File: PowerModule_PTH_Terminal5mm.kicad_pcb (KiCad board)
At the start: 2 copper layers, 26.3 x 20 mm, 5 parts, among them J1 Conn_01x05, J2 Conn_01x05, J3 Screw_Terminal

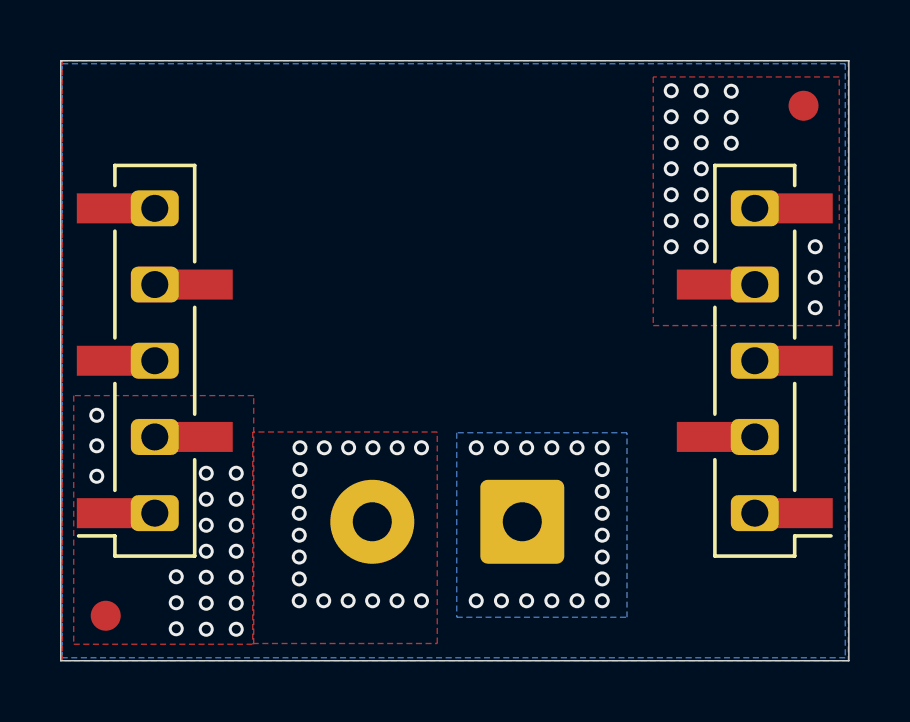
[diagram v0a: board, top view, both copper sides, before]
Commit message: Increase header connectors paste openning by 5%. Decrease screw terminal holes from 2.3mm to 2.2mm.
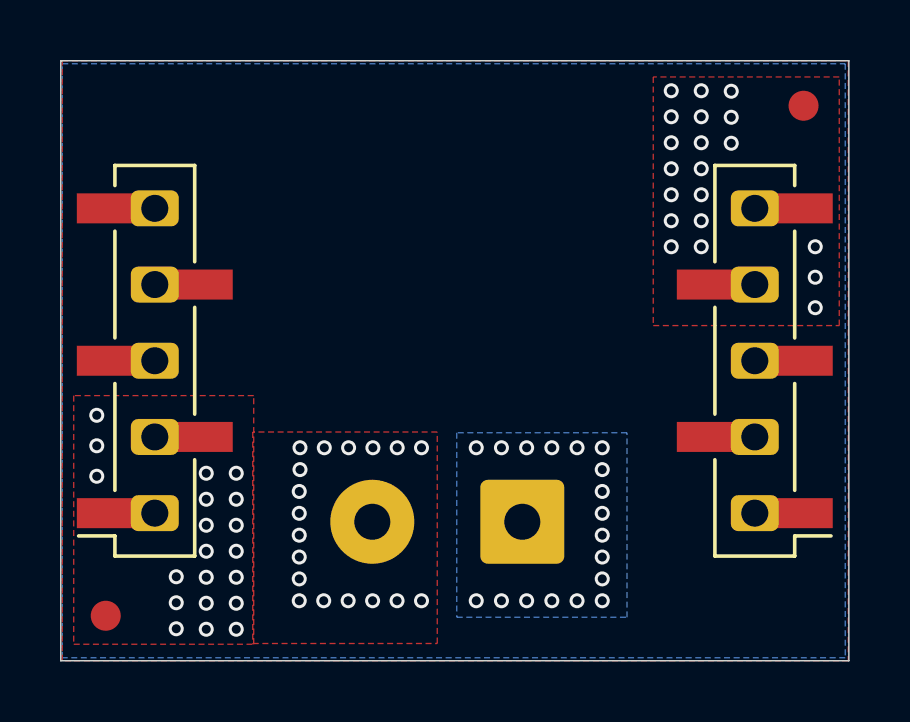
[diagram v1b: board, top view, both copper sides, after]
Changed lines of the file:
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@@
 	(net 3 "unconnected-(J1-Pin_3-Pad3)")
 	(net 4 "unconnected-(J2-Pin_3-Pad3)")
-	(net 5 "unconnected-(J2-Pin_3-Pad3)_1")
-	(net 6 "unconnected-(J1-Pin_3-Pad3)_1")
 	(footprint "Fiducial:Fiducial_1mm_Mask2mm"
 		(locked yes)
@@
 		(sheetname "Root")
 		(sheetfile "PowerModule_PTH_Terminal5mm.kicad_sch")
+		(solder_paste_ratio 0.05)
 		(attr smd)
 		(fp_line
@@
 			(size 1.6 1.2)
 			(drill 0.9)
-			(layers "*.Cu" "*.Mask")
+			(layers "*.Cu" "*.Mask" "In1.Cu" "In2.Cu" "In3.Cu" "In4.Cu" "In5.Cu" "In6.Cu"
+				"In7.Cu" "In8.Cu" "In9.Cu" "In10.Cu" "In11.Cu" "In12.Cu" "In13.Cu" "In14.Cu"
+				"In15.Cu" "In16.Cu" "In17.Cu" "In18.Cu" "In19.Cu" "In20.Cu" "In21.Cu"
+				"In22.Cu" "In23.Cu" "In24.Cu" "In25.Cu" "In26.Cu" "In27.Cu" "In28.Cu"
+				"In29.Cu" "In30.Cu"
+			)
 			(remove_unused_layers no)
 			(roundrect_rratio 0.2083333333)
@@
 			(size 1.6 1.2)
 			(drill 0.9)
-			(layers "*.Cu" "*.Mask")
+			(layers "*.Cu" "*.Mask" "In1.Cu" "In2.Cu" "In3.Cu" "In4.Cu" "In5.Cu" "In6.Cu"
+				"In7.Cu" "In8.Cu" "In9.Cu" "In10.Cu" "In11.Cu" "In12.Cu" "In13.Cu" "In14.Cu"
+				"In15.Cu" "In16.Cu" "In17.Cu" "In18.Cu" "In19.Cu" "In20.Cu" "In21.Cu"
+				"In22.Cu" "In23.Cu" "In24.Cu" "In25.Cu" "In26.Cu" "In27.Cu" "In28.Cu"
+				"In29.Cu" "In30.Cu"
+			)
 			(remove_unused_layers no)
 			(roundrect_rratio 0.2083333333)
@@
 			(size 1.6 1.2)
 			(drill 0.9)
-			(layers "*.Cu" "*.Mask")
+			(layers "*.Cu" "*.Mask" "In1.Cu" "In2.Cu" "In3.Cu" "In4.Cu" "In5.Cu" "In6.Cu"
+				"In7.Cu" "In8.Cu" "In9.Cu" "In10.Cu" "In11.Cu" "In12.Cu" "In13.Cu" "In14.Cu"
+				"In15.Cu" "In16.Cu" "In17.Cu" "In18.Cu" "In19.Cu" "In20.Cu" "In21.Cu"
+				"In22.Cu" "In23.Cu" "In24.Cu" "In25.Cu" "In26.Cu" "In27.Cu" "In28.Cu"
+				"In29.Cu" "In30.Cu"
+			)
 			(remove_unused_layers no)
 			(roundrect_rratio 0.2083333333)
@@
 			(size 1.9 1)
 			(layers "F.Cu" "F.Paste" "F.Mask")
-			(net 6 "unconnected-(J1-Pin_3-Pad3)_1")
+			(net 3 "unconnected-(J1-Pin_3-Pad3)")
 			(pinfunction "Pin_3")
 			(pintype "passive+no_connect")
@@
 			(size 1.6 1.2)
 			(drill 0.9)
-			(layers "*.Cu" "*.Mask")
+			(layers "*.Cu" "*.Mask" "In1.Cu" "In2.Cu" "In3.Cu" "In4.Cu" "In5.Cu" "In6.Cu"
+				"In7.Cu" "In8.Cu" "In9.Cu" "In10.Cu" "In11.Cu" "In12.Cu" "In13.Cu" "In14.Cu"
+				"In15.Cu" "In16.Cu" "In17.Cu" "In18.Cu" "In19.Cu" "In20.Cu" "In21.Cu"
+				"In22.Cu" "In23.Cu" "In24.Cu" "In25.Cu" "In26.Cu" "In27.Cu" "In28.Cu"
+				"In29.Cu" "In30.Cu"
+			)
 			(remove_unused_layers no)
 			(roundrect_rratio 0.2083333333)
@@
 			(size 1.6 1.2)
 			(drill 0.9)
-			(layers "*.Cu" "*.Mask")
+			(layers "*.Cu" "*.Mask" "In1.Cu" "In2.Cu" "In3.Cu" "In4.Cu" "In5.Cu" "In6.Cu"
+				"In7.Cu" "In8.Cu" "In9.Cu" "In10.Cu" "In11.Cu" "In12.Cu" "In13.Cu" "In14.Cu"
+				"In15.Cu" "In16.Cu" "In17.Cu" "In18.Cu" "In19.Cu" "In20.Cu" "In21.Cu"
+				"In22.Cu" "In23.Cu" "In24.Cu" "In25.Cu" "In26.Cu" "In27.Cu" "In28.Cu"
+				"In29.Cu" "In30.Cu"
+			)
 			(remove_unused_layers no)
 			(roundrect_rratio 0.2083333333)
@@
 		(sheetname "Root")
 		(sheetfile "PowerModule_PTH_Terminal5mm.kicad_sch")
+		(solder_paste_ratio 0.05)
 		(attr smd)
 		(fp_line
@@
 			(size 1.6 1.2)
 			(drill 0.9)
-			(layers "*.Cu" "*.Mask")
+			(layers "*.Cu" "*.Mask" "In1.Cu" "In2.Cu" "In3.Cu" "In4.Cu" "In5.Cu" "In6.Cu"
+				"In7.Cu" "In8.Cu" "In9.Cu" "In10.Cu" "In11.Cu" "In12.Cu" "In13.Cu" "In14.Cu"
+				"In15.Cu" "In16.Cu" "In17.Cu" "In18.Cu" "In19.Cu" "In20.Cu" "In21.Cu"
+				"In22.Cu" "In23.Cu" "In24.Cu" "In25.Cu" "In26.Cu" "In27.Cu" "In28.Cu"
+				"In29.Cu" "In30.Cu"
+			)
 			(remove_unused_layers no)
 			(roundrect_rratio 0.2083333333)
@@
 			(size 1.6 1.2)
 			(drill 0.9)
-			(layers "*.Cu" "*.Mask")
+			(layers "*.Cu" "*.Mask" "In1.Cu" "In2.Cu" "In3.Cu" "In4.Cu" "In5.Cu" "In6.Cu"
+				"In7.Cu" "In8.Cu" "In9.Cu" "In10.Cu" "In11.Cu" "In12.Cu" "In13.Cu" "In14.Cu"
+				"In15.Cu" "In16.Cu" "In17.Cu" "In18.Cu" "In19.Cu" "In20.Cu" "In21.Cu"
+				"In22.Cu" "In23.Cu" "In24.Cu" "In25.Cu" "In26.Cu" "In27.Cu" "In28.Cu"
+				"In29.Cu" "In30.Cu"
+			)
 			(remove_unused_layers no)
 			(roundrect_rratio 0.2083333333)
@@
 			(size 1.6 1.2)
 			(drill 0.9)
-			(layers "*.Cu" "*.Mask")
+			(layers "*.Cu" "*.Mask" "In1.Cu" "In2.Cu" "In3.Cu" "In4.Cu" "In5.Cu" "In6.Cu"
+				"In7.Cu" "In8.Cu" "In9.Cu" "In10.Cu" "In11.Cu" "In12.Cu" "In13.Cu" "In14.Cu"
+				"In15.Cu" "In16.Cu" "In17.Cu" "In18.Cu" "In19.Cu" "In20.Cu" "In21.Cu"
+				"In22.Cu" "In23.Cu" "In24.Cu" "In25.Cu" "In26.Cu" "In27.Cu" "In28.Cu"
+				"In29.Cu" "In30.Cu"
+			)
 			(remove_unused_layers no)
 			(roundrect_rratio 0.2083333333)
-			(net 5 "unconnected-(J2-Pin_3-Pad3)_1")
+			(net 4 "unconnected-(J2-Pin_3-Pad3)")
 			(pinfunction "Pin_3")
 			(pintype "passive+no_connect")
@@
 			(size 1.6 1.2)
 			(drill 0.9)
-			(layers "*.Cu" "*.Mask")
+			(layers "*.Cu" "*.Mask" "In1.Cu" "In2.Cu" "In3.Cu" "In4.Cu" "In5.Cu" "In6.Cu"
+				"In7.Cu" "In8.Cu" "In9.Cu" "In10.Cu" "In11.Cu" "In12.Cu" "In13.Cu" "In14.Cu"
+				"In15.Cu" "In16.Cu" "In17.Cu" "In18.Cu" "In19.Cu" "In20.Cu" "In21.Cu"
+				"In22.Cu" "In23.Cu" "In24.Cu" "In25.Cu" "In26.Cu" "In27.Cu" "In28.Cu"
+				"In29.Cu" "In30.Cu"
+			)
 			(remove_unused_layers no)
 			(roundrect_rratio 0.2083333333)
@@
 			(size 1.6 1.2)
 			(drill 0.9)
-			(layers "*.Cu" "*.Mask")
+			(layers "*.Cu" "*.Mask" "In1.Cu" "In2.Cu" "In3.Cu" "In4.Cu" "In5.Cu" "In6.Cu"
+				"In7.Cu" "In8.Cu" "In9.Cu" "In10.Cu" "In11.Cu" "In12.Cu" "In13.Cu" "In14.Cu"
+				"In15.Cu" "In16.Cu" "In17.Cu" "In18.Cu" "In19.Cu" "In20.Cu" "In21.Cu"
+				"In22.Cu" "In23.Cu" "In24.Cu" "In25.Cu" "In26.Cu" "In27.Cu" "In28.Cu"
+				"In29.Cu" "In30.Cu"
+			)
 			(remove_unused_layers no)
 			(roundrect_rratio 0.2083333333)
@@
 			(at 0 0 180)
 			(size 2.8 2.8)
-			(drill 1.3)
-			(layers "*.Cu" "*.Mask")
+			(drill 1.2)
+			(layers "*.Cu" "*.Mask" "In1.Cu" "In2.Cu" "In3.Cu" "In4.Cu" "In5.Cu" "In6.Cu"
+				"In7.Cu" "In8.Cu" "In9.Cu" "In10.Cu" "In11.Cu" "In12.Cu" "In13.Cu" "In14.Cu"
+				"In15.Cu" "In16.Cu" "In17.Cu" "In18.Cu" "In19.Cu" "In20.Cu" "In21.Cu"
+				"In22.Cu" "In23.Cu" "In24.Cu" "In25.Cu" "In26.Cu" "In27.Cu" "In28.Cu"
+				"In29.Cu" "In30.Cu"
+			)
 			(remove_unused_layers no)
 			(roundrect_rratio 0.089286)
@@
 			(at 5 0 180)
 			(size 2.8 2.8)
-			(drill 1.3)
-			(layers "*.Cu" "*.Mask")
+			(drill 1.2)
+			(layers "*.Cu" "*.Mask" "In1.Cu" "In2.Cu" "In3.Cu" "In4.Cu" "In5.Cu" "In6.Cu"
+				"In7.Cu" "In8.Cu" "In9.Cu" "In10.Cu" "In11.Cu" "In12.Cu" "In13.Cu" "In14.Cu"
+				"In15.Cu" "In16.Cu" "In17.Cu" "In18.Cu" "In19.Cu" "In20.Cu" "In21.Cu"
+				"In22.Cu" "In23.Cu" "In24.Cu" "In25.Cu" "In26.Cu" "In27.Cu" "In28.Cu"
+				"In29.Cu" "In30.Cu"
+			)
 			(remove_unused_layers no)
 			(net 1 "GND")
